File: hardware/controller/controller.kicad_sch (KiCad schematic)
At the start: 0 parts

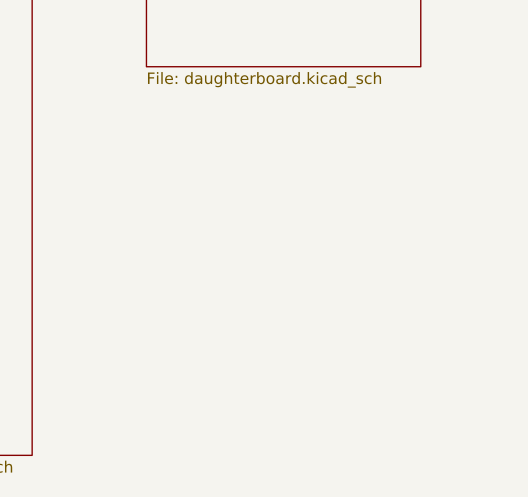
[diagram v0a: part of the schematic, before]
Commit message: feat(controller): VBUS protection F1/D1, TPD4E05U06 symbol, ERC power flags (I3)
- F1 SMD1210-110-24V (C22436715), D1 SMF20A (C123788) as D_Zener_Small, cathode on DB_VBUS
- U3 on new ibm_m:TPD4E05U06DQA symbol, connections unchanged
- ERC sheet with PWR_FLAG for VBUS, VBAT, PVSS2, DB_VBUS, DB_GND
- C19 footprint 0402
- docs: I3 applied, J2 = JST PH, WS2812C VIH resolved
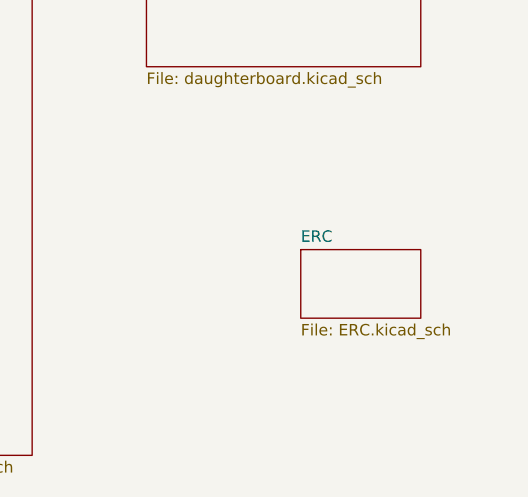
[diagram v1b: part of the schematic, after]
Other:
- added sheet ERC (ERC.kicad_sch)
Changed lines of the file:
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@@
+		)
+	)
+	(sheet
+		(at 144.145 100.33)
+		(size 13.335 7.62)
+		(exclude_from_sim no)
+		(in_bom yes)
+		(on_board yes)
+		(dnp no)
+		(fields_autoplaced yes)
+		(stroke
+			(width 0.1524)
+			(type solid)
+		)
+		(fill
+			(color 0 0 0 0)
+		)
+		(property "Sheetname" "ERC"
+			(at 144.145 99.6184 0)
+			(show_name no)
+			(do_not_autoplace no)
+			(effects
+				(font
+					(size 1.27 1.27)
+				)
+				(justify left bottom)
+			)
+		)
+		(property "Sheetfile" "ERC.kicad_sch"
+			(at 144.145 108.5346 0)
+			(show_name no)
+			(do_not_autoplace no)
+			(effects
+				(font
+					(size 1.27 1.27)
+				)
+				(justify left top)
+			)
+		)
+		(instances
+			(project "controller"
+				(path "/17f6a4a5-fbff-4e30-a1cc-9481373e4968"
+					(page "4")
+				)
+			)
 		)
 	)

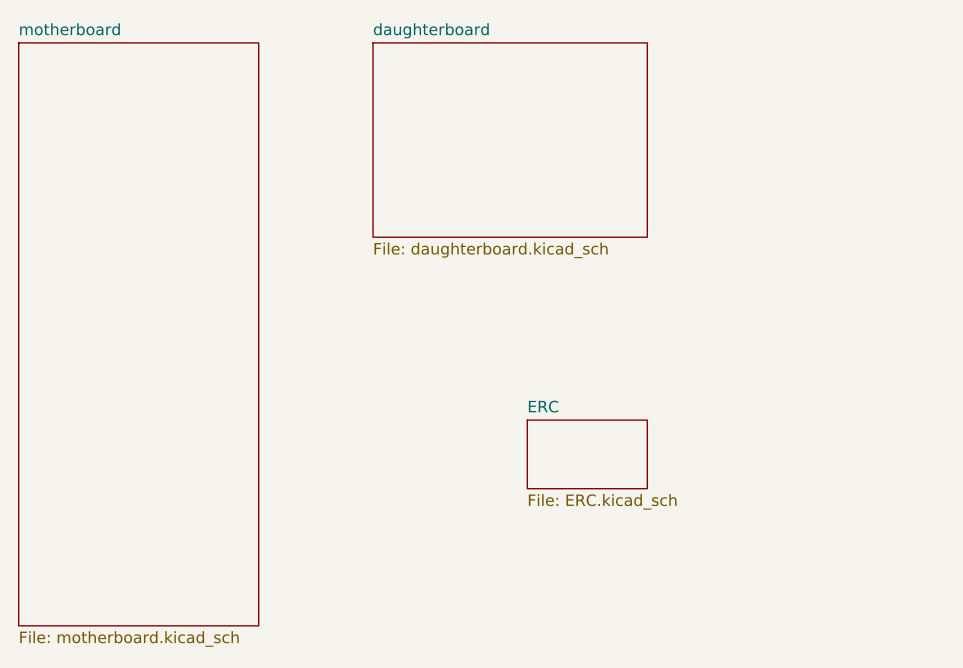
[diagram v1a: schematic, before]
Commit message: feat(controller): split schematic into pages, JLC BOM, RF config 7 (A13, A14, M5, P9)
- Schematic split into Power, MCU Core, MCU IO and Daughterboard pages;
  motherboard.kicad_sch and ERC.kicad_sch removed, cross-page signals as
  global labels. J3 pins 1-3 fixed (local labels did not join power nets).
- R1/R2 0R in series with SCL/SDA to J3.
- RF matching per nRF52840 reference config 7 (C3 1.0p, L1 4.7n, C4 1.2p,
  L5 2.2n), C22 removed.
- BOM for JLC assembly: passives moved to basic parts, R10 LCSC fixed
  (470k 0603), C16 0603, C9 DNP; Q2 AO3401A (new ibm_m symbol);
  SW1 TS-1187A-B-A-B; D2 WS2812B-2020-V6; J6 U.FL-IPEX-1 (pads renumbered).
- ERC 0 errors / 0 warnings; tools/kicad-check.sh runs ERC, netlist, PDF.
- Docs: CHANGELOG A13/A14, M5, P9; HARDWARE_DECISIONS BOM table; CLAUDE.md.
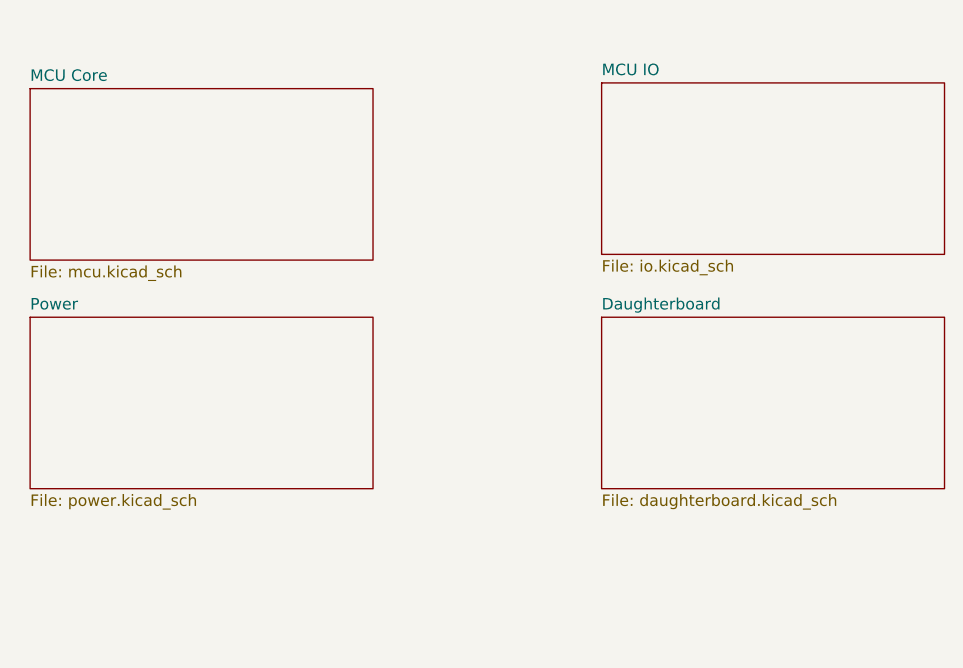
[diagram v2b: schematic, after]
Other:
- sheet daughterboard renamed Daughterboard
- sheet motherboard renamed MCU Core
- removed sheet ERC
- added sheet MCU IO (io.kicad_sch)
- added sheet Power (power.kicad_sch)
- sheet MCU Core: file motherboard.kicad_sch -> mcu.kicad_sch
- title: (none) -> IBM Model M Controller
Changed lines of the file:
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@@
 	(generator_version "10.0")
 	(paper "A4")
+	(title_block
+		(title "IBM Model M Controller")
+		(date "2026-10-25")
+		(rev "1")
+	)
 	(sheet
-		(at 87.63 58.42)
-		(size 26.67 64.77)
+		(at 88.9 63.5)
+		(size 38.1 19.05)
 		(exclude_from_sim no)
 		(in_bom yes)
@@
 			(color 0 0 0 0)
 		)
-		(property "Sheetname" "motherboard"
-			(at 87.63 57.7084 0)
+		(property "Sheetname" "MCU Core"
+			(at 88.9 62.7884 0)
 			(show_name no)
 			(do_not_autoplace no)
@@
 			)
 		)
-		(property "Sheetfile" "motherboard.kicad_sch"
-			(at 87.63 123.7746 0)
+		(property "Sheetfile" "mcu.kicad_sch"
+			(at 88.9 83.1346 0)
 			(show_name no)
 			(do_not_autoplace no)
@@
 	)
 	(sheet
-		(at 127 58.42)
-		(size 30.48 21.59)
+		(at 152.4 62.865)
+		(size 38.1 19.05)
 		(exclude_from_sim no)
 		(in_bom yes)
@@
 			(color 0 0 0 0)
 		)
-		(property "Sheetname" "daughterboard"
-			(at 127 57.7084 0)
+		(property "Sheetname" "MCU IO"
+			(at 152.4 62.1534 0)
 			(show_name no)
 			(do_not_autoplace no)
@@
 			)
 		)
-		(property "Sheetfile" "daughterboard.kicad_sch"
-			(at 127 80.5946 0)
+		(property "Sheetfile" "io.kicad_sch"
+			(at 152.4 82.4996 0)
 			(show_name no)
 			(do_not_autoplace no)
@@
 	)
 	(sheet
-		(at 144.145 100.33)
-		(size 13.335 7.62)
+		(at 152.4 88.9)
+		(size 38.1 19.05)
 		(exclude_from_sim no)
 		(in_bom yes)
@@
 			(color 0 0 0 0)
 		)
-		(property "Sheetname" "ERC"
-			(at 144.145 99.6184 0)
+		(property "Sheetname" "Daughterboard"
+			(at 152.4 88.1884 0)
 			(show_name no)
 			(do_not_autoplace no)
@@
 			)
 		)
-		(property "Sheetfile" "ERC.kicad_sch"
-			(at 144.145 108.5346 0)
+		(property "Sheetfile" "daughterboard.kicad_sch"
+			(at 152.4 108.5346 0)
 			(show_name no)
 			(do_not_autoplace no)
@@
 		)
 	)
+	(sheet
+		(at 88.9 88.9)
+		(size 38.1 19.05)
+		(exclude_from_sim no)
+		(in_bom yes)
+		(on_board yes)
+		(dnp no)
+		(fields_autoplaced yes)
+		(stroke
+			(width 0.1524)
+			(type solid)
+		)
+		(fill
+			(color 0 0 0 0)
+		)
+		(property "Sheetname" "Power"
+			(at 88.9 88.1884 0)
+			(show_name no)
+			(do_not_autoplace no)
+			(effects
+				(font
+					(size 1.27 1.27)
+				)
+				(justify left bottom)
+			)
+		)
+		(property "Sheetfile" "power.kicad_sch"
+			(at 88.9 108.5346 0)
+			(show_name no)
+			(do_not_autoplace no)
+			(effects
+				(font
+					(size 1.27 1.27)
+				)
+				(justify left top)
+			)
+		)
+		(instances
+			(project "controller"
+				(path "/17f6a4a5-fbff-4e30-a1cc-9481373e4968"
+					(page "1")
+				)
+			)
+		)
+	)
 	(sheet_instances
 		(path "/"
-			(page "1")
+			(page "0")
 		)
 	)
